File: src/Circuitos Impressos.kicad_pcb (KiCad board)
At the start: 2 copper layers, 145 parts, among them J1 SM03B-SRSS-TB, J2 USB_C_Receptacle_USB2.0_14P, J3 Micro_SD_Card, J4 Conn_02x15_Odd_Even, J5 USB_C_Receptacle_USB2.0_14P, Q1 Q_NMOS_SGD, Q2 Q_NMOS_GSD, Q5 NPN, Q6 Q_NMOS_SGD, SW5 SW_Push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

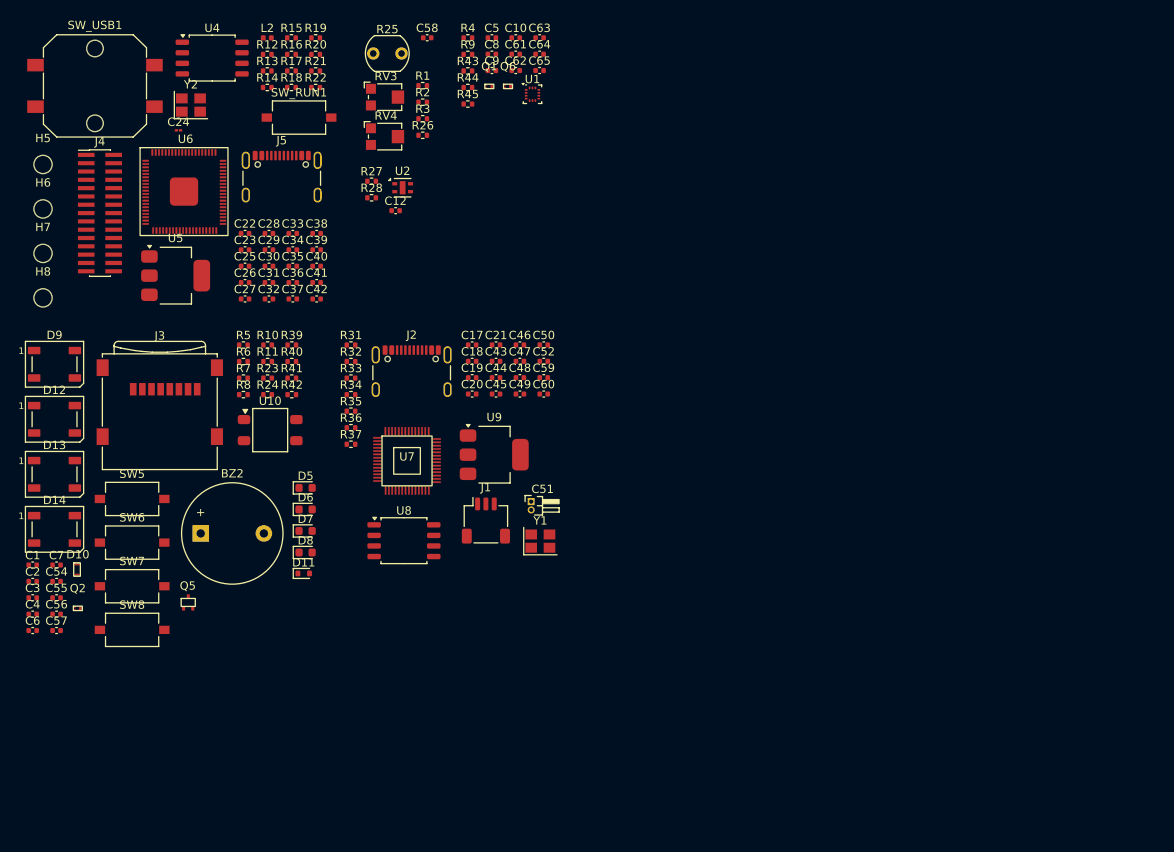
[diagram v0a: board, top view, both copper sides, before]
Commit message: Bugs na att da PCI resolvidos (falta só a tela OLED)
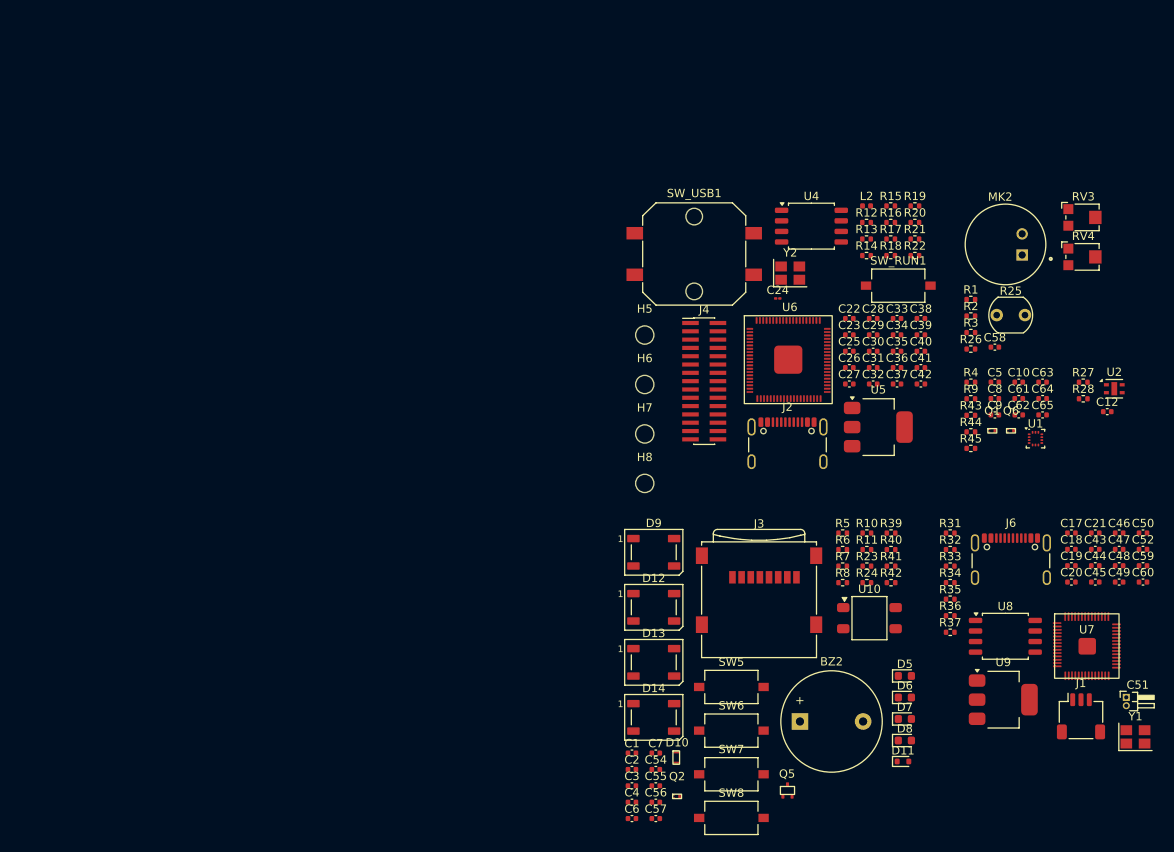
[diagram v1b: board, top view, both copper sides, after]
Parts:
- removed J5: USB_C_Receptacle_USB2.0_14P, Connector_USB:USB_C_Receptacle_GCT_USB4105-xx-A_16P_TopMnt_Horizontal
- added J6: USB_C_Receptacle_USB2.0_16P, Connector_USB:USB_C_Receptacle_GCT_USB4105-xx-A_16P_TopMnt_Horizontal, F.Cu at (189.3, 122.4)
- added MK2: CMA-4544PF-W, componentes_personalizados:MIC_CMA-4544PF-W, F.Cu at (188.7, 83.4)
- J2: value USB_C_Receptacle_USB2.0_14P -> USB_C_Receptacle_USB2.0_16P
- moved R27 89.0 mm to (198.0, 99.9)
- moved R28 89.0 mm to (198.0, 101.9)
- moved C12 89.0 mm to (200.9, 103.5)
- moved U2 89.0 mm to (201.8, 100.7)
- moved U5 86.5 mm to (173.4, 105.3)
- moved RV3 85.1 mm to (198.0, 80.1)
- moved RV4 85.1 mm to (198.0, 84.9)
- moved U7 84.8 mm to (198.4, 131.7)
- moved R25 81.3 mm to (187.6, 91.9)
- moved C58 77.8 mm to (187.4, 95.7)
- moved H8 75.8 mm to (145.3, 112.1)
- moved H7 75.6 mm to (145.3, 106.2)
- moved BZ2 75.6 mm to (163.9, 140.8)
- moved C43 75.6 mm to (199.5, 120.0)
- moved C44 75.6 mm to (199.5, 122.0)
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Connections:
- J1 pad 3: SWD -> SWDIO
- J2 pad A6: /debugger_RP2040/USB_D+ -> /MCU_RP2350/USB_D+
- J2 pad A7: /debugger_RP2040/USB_D- -> /MCU_RP2350/USB_D-
- J2 pad A8: (no net) -> unconnected-(J2-SBU1-PadA8)
- J2 pad B6: /debugger_RP2040/USB_D+ -> /MCU_RP2350/USB_D+
- J2 pad B7: /debugger_RP2040/USB_D- -> /MCU_RP2350/USB_D-
- J2 pad B8: (no net) -> unconnected-(J2-SBU2-PadB8)
- R15 pad 2: Net-(J5-CC1) -> Net-(J2-CC1)
- R16 pad 2: Net-(J5-CC2) -> Net-(J2-CC2)
- R35 pad 2: Net-(J2-CC1) -> Net-(J6-CC1)
- R36 pad 2: Net-(J2-CC2) -> Net-(J6-CC2)

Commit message: Subconjuntos organizados na PCI
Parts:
- added L3: ~, Display:OLED-128O064D, F.Cu at (260.2, 36.7)
- SW_USB1: footprint Button_Switch_SMD:SW_Push_1P1T_NO_CK_PTS125Sx43PSMTR -> Button_Switch_SMD:SW_Tactile_SPST_NO_Straight_CK_PTS636Sx25SMTRLFS
- moved C6 182.1 mm to (14.4, 24.2)
- moved C55 176.3 mm to (14.1, 32.2)
- moved C56 172.3 mm to (14.1, 40.4)
- moved C57 168.7 mm to (14.2, 47.9)
- moved D11 159.7 mm to (51.8, 45.6)
- moved D9 157.8 mm to (19.0, 27.3)
- moved BZ2 157.3 mm to (45.4, 37.4)
- moved D12 157.2 mm to (18.7, 35.3)
- moved D13 156.3 mm to (18.7, 43.4)
- moved D14 155.7 mm to (18.9, 51.0)
- moved Q5 152.3 mm to (48.8, 47.6), turned to 180 degrees
- moved R23 146.8 mm to (46.6, 45.8)
- moved Q2 134.1 mm to (72.2, 42.9)
- moved J3 133.3 mm to (32.2, 165.9)
- moved R11 129.3 mm to (70.5, 40.0), turned to -90 degrees
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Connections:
- U7 pad 20: unconnected-(U7-XIN-Pad20) -> /debugger_RP2040/XIN
- U7 pad 21: unconnected-(U7-XOUT-Pad21) -> /debugger_RP2040/XOUT
- U7 pad 51: unconnected-(U7-QSPI_SD3-Pad51) -> /debugger_RP2040/QSPI_SD3
- U7 pad 52: unconnected-(U7-QSPI_SCLK-Pad52) -> /debugger_RP2040/QSPI_SCLK
- U7 pad 53: unconnected-(U7-QSPI_SD0-Pad53) -> /debugger_RP2040/QSPI_SD0
- U7 pad 54: unconnected-(U7-QSPI_SD2-Pad54) -> /debugger_RP2040/QSPI_SD2
- U7 pad 55: unconnected-(U7-QSPI_SD1-Pad55) -> /debugger_RP2040/QSPI_SD1
- U7 pad 56: unconnected-(U7-QSPI_SS-Pad56) -> /debugger_RP2040/QSPI_SS
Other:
- board text added: "LDR"
- board text added: "Power_rp2040"
- board text added: "RP2040"
- board text added: "acell"
- board text added: "botões tácteis"
- board text added: "buzzer"
- board text added: "crystal_rp2040"
- board text added: "emissor e receptor IR"
- board text added: "flash_rp2040"
- board text added: "led rgb"
- board text added: "leds mono"
- board text added: "microSD"
- board text added: "microfone"
- board text added: "mosfet"
- board text added: "rp2350"
- board text added: "tela oled"
- board text added: "trimpots"
- board text added: "umid_temp"

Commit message: placement finalizado, faltando trilhas
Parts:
- moved C7 162.0 mm to (151.6, 45.6)
- moved J3 162.0 mm to (142.4, 47.2)
- moved C55 150.5 mm to (137.7, 118.0)
- moved C56 150.5 mm to (137.7, 126.2)
- moved C6 150.5 mm to (138.0, 110.0)
- moved D12 150.5 mm to (142.3, 121.1)
- moved D9 150.5 mm to (142.6, 113.1)
- moved D13 150.5 mm to (142.3, 129.2)
- moved C57 150.3 mm to (137.7, 133.7)
- moved D14 150.3 mm to (142.3, 136.7)
- moved H7 139.0 mm to (117.8, 136.6)
- moved H6 129.5 mm to (117.8, 44.7)
- moved R9 125.2 mm to (163.1, 116.6)
- moved C63 125.2 mm to (167.8, 118.9)
- moved C64 125.2 mm to (152.0, 118.9)
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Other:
- board outline added: 76.3 x 99.3 mm
- copper layers 2 -> 4
- board text removed: "LDR"
- board text removed: "Power_rp2040"
- board text removed: "RP2040"
- board text removed: "acell"
- board text removed: "botões tácteis"
- board text removed: "buzzer"
- board text removed: "crystal_rp2040"
- board text removed: "emissor e receptor IR"
- board text removed: "flash_rp2040"
- board text removed: "led rgb"
- board text removed: "leds mono"
- board text removed: "microSD"
- board text removed: "microfone"
- board text removed: "mosfet"
- board text removed: "rp2350"
- board text removed: "tela oled"
- board text removed: "trimpots"
- board text removed: "umid_temp"

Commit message: FEAT: Trilhas parcialmente adicionadas
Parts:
- removed Q5: NPN, componentes_personalizados:transistor - DTC014E SOT-416FL
- moved U6 0.58 mm to (168.5, 83.6)
- moved R32 0.31 mm to (134.3, 77.0), turned to 90 degrees
- moved R33 0.25 mm to (133.0, 77.0), turned to 90 degrees
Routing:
- net +3V3: track 0.00 -> 386.7 mm, vias 0 -> 2
- net VBUS: track 0.00 -> 184.4 mm, vias 0 -> 2
- net Net-(U7-ADC_AVDD): track 0.00 -> 80.1 mm, vias 0 -> 2
- net +1V1: track 0.00 -> 44.9 mm, vias 0 -> 2
- net /MCU_RP2350/USB_D-: track 0.00 -> 34.2 mm, vias 0 -> 2
- net /debugger_RP2040/QSPI_SS: track 0.00 -> 27.9 mm, vias 0 -> 2
- net /debugger_RP2040/QSPI_SCLK: track 0.00 -> 26.4 mm
- net VDD: track 0.00 -> 23.4 mm
- net /debugger_RP2040/QSPI_SD1: track 0.00 -> 20.1 mm, vias 0 -> 2
- net /debugger_RP2040/QSPI_SD3: track 0.00 -> 19.8 mm, vias 0 -> 2
- net /debugger_RP2040/QSPI_SD0: track 0.00 -> 19.6 mm, vias 0 -> 2
- net Net-(C43-Pad2): track 0.00 -> 16.9 mm
- net SWCLK: track 0.00 -> 13.6 mm, vias 0 -> 2
- net /debugger_RP2040/QSPI_SD2: track 0.00 -> 12.6 mm, vias 0 -> 2
- net Net-(U9-VO): track 0.00 -> 11.5 mm, vias 0 -> 3
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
